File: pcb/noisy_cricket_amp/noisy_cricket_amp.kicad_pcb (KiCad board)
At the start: 2 copper layers, 23 parts, among them J1 AudioJack2, J2 AudioJack2, J3 Jack-DC, Q1 MPF102, SW1 SW_SPST, SW2 SW_SPST, U1 LM386

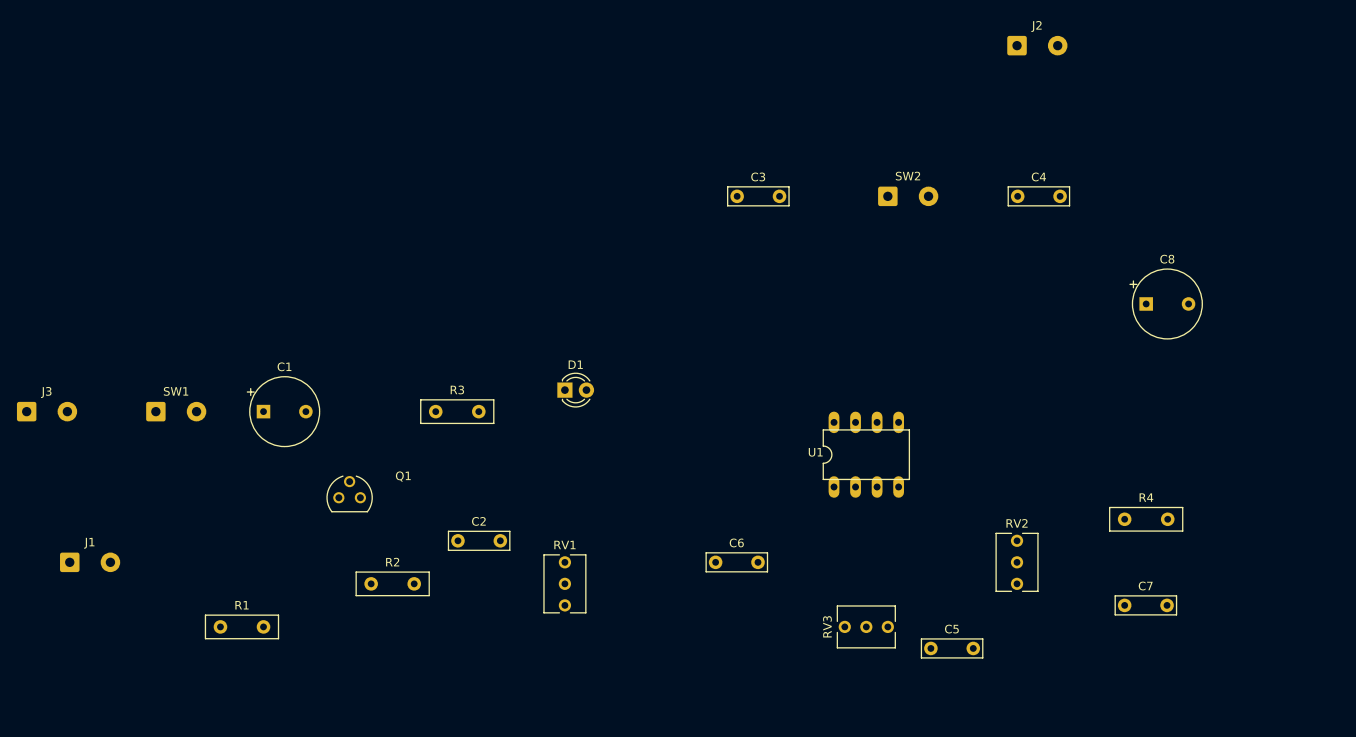
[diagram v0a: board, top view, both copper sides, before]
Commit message: Adding p10 output connector and initial pcb placement
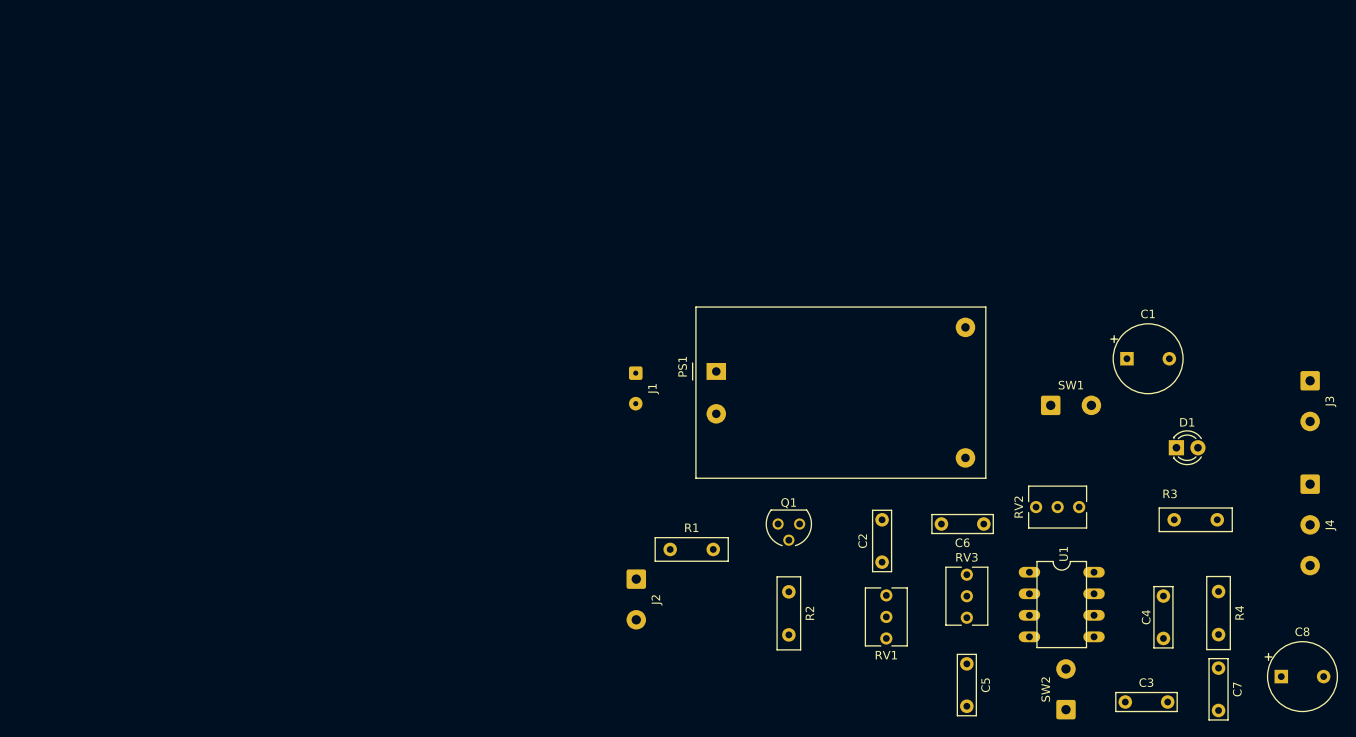
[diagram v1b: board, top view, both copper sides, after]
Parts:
- added J4: AudioJack2_SwitchT, Connector_Wire:SolderWire-0.5sqmm_1x03_P4.8mm_D0.9mm_OD2.3mm, F.Cu at (220.0, 87.3)
- added PS1: HLK-PM12, Converter_ACDC:Converter_ACDC_HiLink_HLK-PMxx, F.Cu at (149.9, 74.0)
- J1: value AudioJack2 -> Conn_01x02_Male; footprint Connector_Wire:SolderWire-0.5sqmm_1x02_P4.8mm_D0.9mm_OD2.3mm -> Connector_Wire:SolderWire-0.1sqmm_1x02_P3.6mm_D0.4mm_OD1mm
- J3: value Jack-DC -> AudioJack2
- moved J3 151.5 mm to (220.0, 75.1), turned to -90 degrees
- moved SW1 105.6 mm to (189.4, 78.0)
- moved C1 102.1 mm to (198.4, 72.5)
- moved R3 88.1 mm to (204.0, 91.5)
- moved J2 77.3 mm to (140.5, 98.5), turned to -90 degrees
- moved C3 75.2 mm to (198.2, 113.0)
- moved D1 72.5 mm to (204.2, 83.0)
- moved J1 70.4 mm to (140.4, 74.2), turned to -90 degrees
- moved SW2 64.1 mm to (191.2, 113.9), turned to 90 degrees
- moved C4 54.9 mm to (202.7, 105.5), turned to 90 degrees
- moved R1 53.8 mm to (144.5, 95.0)
- moved Q1 51.9 mm to (158.5, 92.0), turned to 180 degrees
- moved C2 50.1 mm to (169.5, 96.5), turned to 90 degrees
- moved R2 49.3 mm to (158.5, 100.0), turned to -90 degrees
- moved C8 46.8 mm to (216.6, 110.0)
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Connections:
- J2 pad T: Net-(C8-Pad2) -> Net-(J2-PadT)
- Q1 pad 3: Net-(Q1-Pad3) -> Net-(J2-PadT)
- R1 pad 1: Net-(Q1-Pad3) -> Net-(J2-PadT)
- SW1 pad 1: Net-(J3-Pad1) -> Net-(PS1-Pad4)

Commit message: Routing component trails
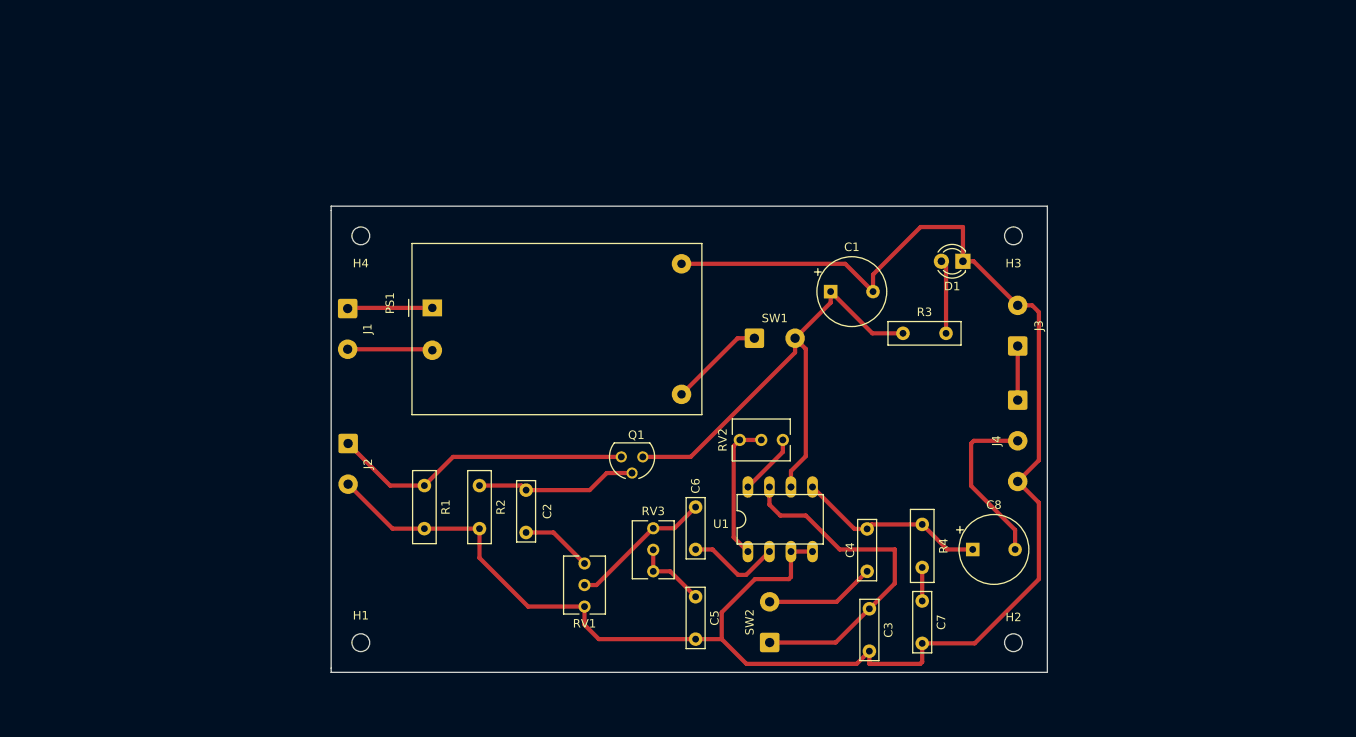
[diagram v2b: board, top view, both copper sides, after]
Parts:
- added H1: MountingHole, MountingHole:MountingHole_2.1mm, F.Cu at (108.0, 106.0)
- added H2: MountingHole, MountingHole:MountingHole_2.1mm, F.Cu at (185.0, 106.0)
- added H3: MountingHole, MountingHole:MountingHole_2.1mm, F.Cu at (185.0, 58.0)
- added H4: MountingHole, MountingHole:MountingHole_2.1mm, F.Cu at (108.0, 58.0)
- J1: footprint Connector_Wire:SolderWire-0.1sqmm_1x02_P3.6mm_D0.4mm_OD1mm -> Connector_Wire:SolderWire-0.5sqmm_1x02_P4.8mm_D0.9mm_OD2.3mm
- moved C2 42.1 mm to (127.5, 93.0)
- moved C8 39.4 mm to (180.2, 95.0)
- moved R3 38.8 mm to (172.0, 69.5)
- moved R2 38.6 mm to (122.0, 87.5)
- moved J2 37.6 mm to (106.5, 82.5)
- moved RV3 37.4 mm to (142.5, 92.5)
- moved J4 35.9 mm to (185.5, 77.4)
- moved C1 35.8 mm to (163.4, 64.6)
- moved RV2 35.8 mm to (152.7, 82.1)
- moved SW1 35.8 mm to (154.4, 70.1)
- moved C4 35.8 mm to (167.7, 97.6)
- moved C7 35.8 mm to (174.2, 101.1)
- moved R4 35.8 mm to (174.2, 92.0)
- moved SW2 35.8 mm to (156.2, 106.0)
- moved RV1 35.8 mm to (134.4, 101.7)
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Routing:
- net GND: track 0.00 -> 207.7 mm
- net Net-(C1-Pad1): track 0.00 -> 61.7 mm
- net Net-(C3-Pad1): track 0.00 -> 42.0 mm
- net Net-(J2-PadT): track 0.00 -> 35.7 mm
- net Net-(C4-Pad2): track 0.00 -> 22.4 mm
- net Net-(C8-Pad2): track 0.00 -> 20.3 mm
- net Net-(C2-Pad2): track 0.00 -> 19.1 mm
- net Net-(C6-Pad2): track 0.00 -> 16.9 mm
- net Net-(RV2-Pad1): track 0.00 -> 16.7 mm
- net Net-(C4-Pad1): track 0.00 -> 13.0 mm
- net Net-(PS1-Pad4): track 0.00 -> 11.3 mm
- net Net-(C6-Pad1): track 0.00 -> 11.1 mm
- net Net-(J1-Pad2): track 0.00 -> 10.0 mm
- net Net-(J1-Pad1): track 0.00 -> 10.0 mm
- net Net-(C5-Pad1): track 0.00 -> 8.78 mm
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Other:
- board outline added: 84.5 x 55 mm

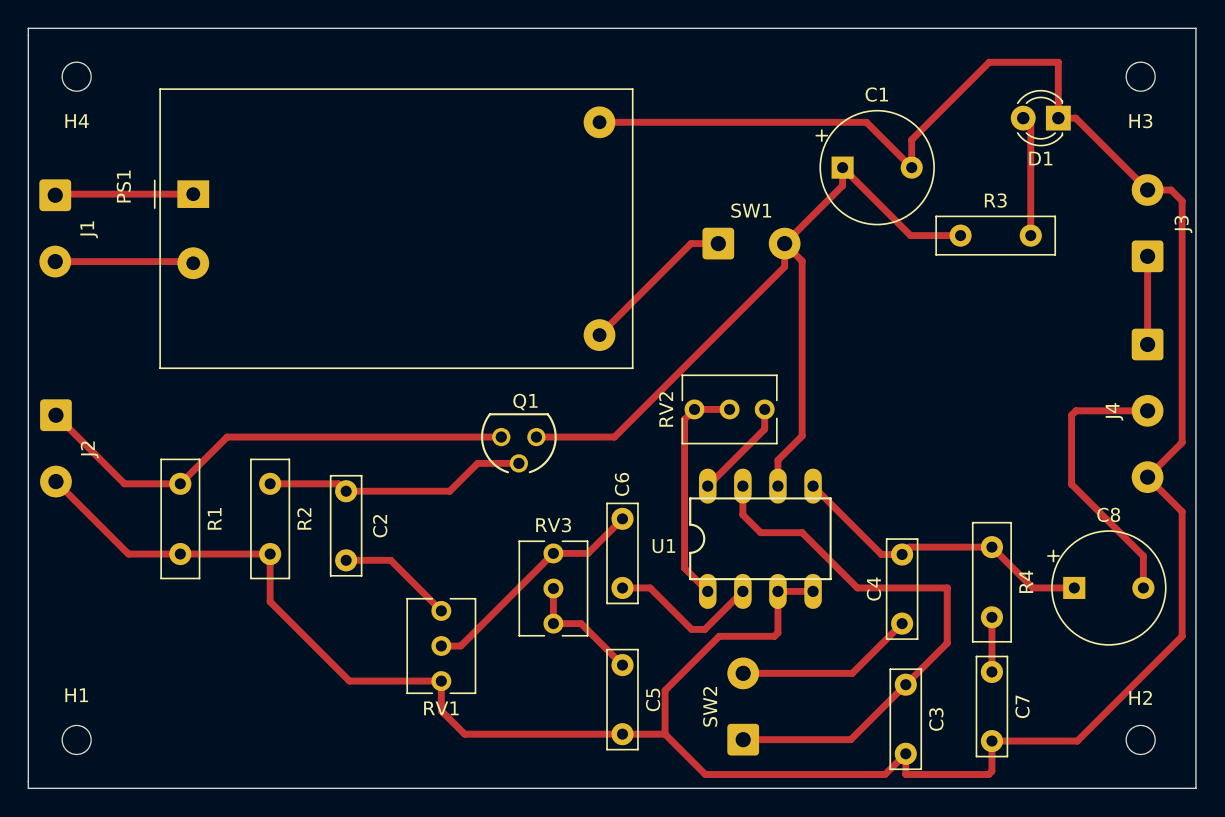
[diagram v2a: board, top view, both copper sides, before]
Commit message: Holes for battery and layout improvements
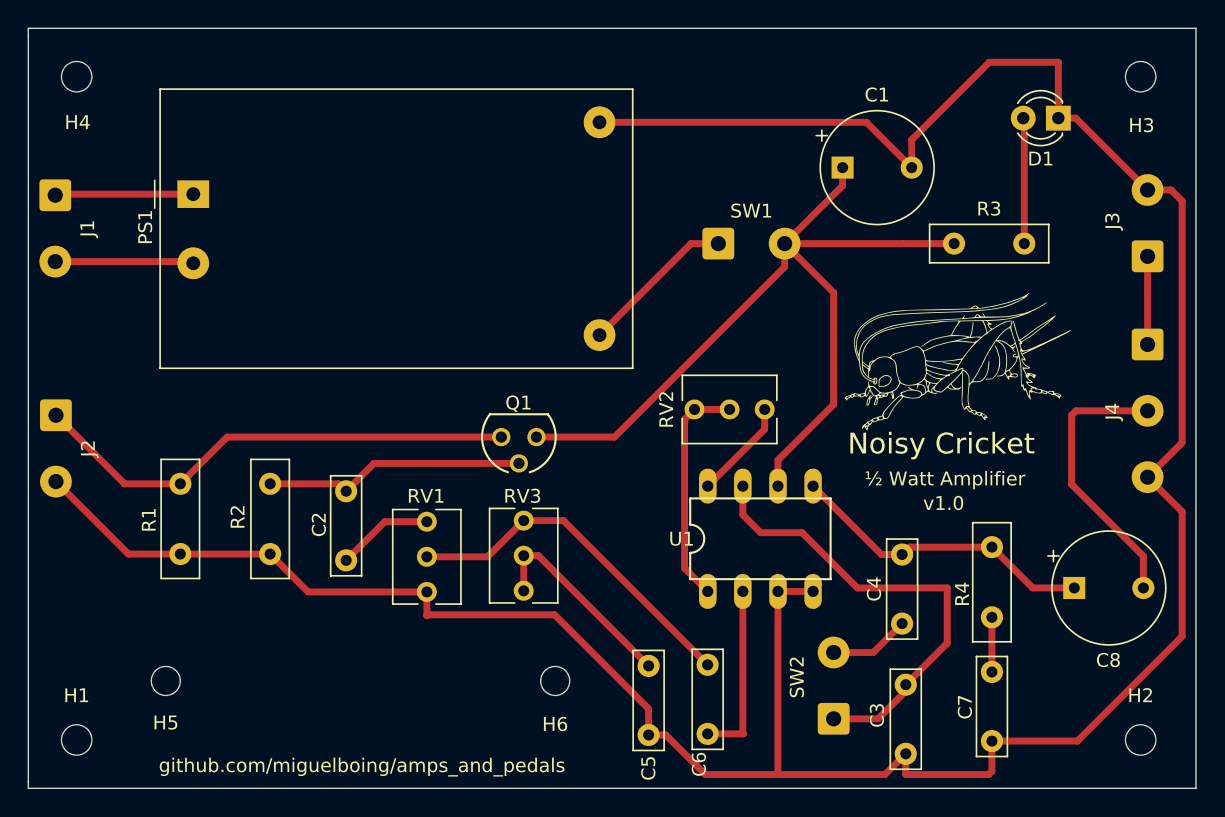
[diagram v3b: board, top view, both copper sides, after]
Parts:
- added G***: LOGO, logo:logo, F.Cu at (171.5, 79.4)
- added H5: MountingHole_Pad, MountingHole:MountingHole_2.1mm, F.Cu at (114.5, 101.7)
- added H6: MountingHole_Pad, MountingHole:MountingHole_2.1mm, F.Cu at (142.6, 101.7)
- H1, H2, H3, H4: footprint MountingHole:MountingHole_2.1mm -> MountingHole:MountingHole_2.2mm_M2
- moved C6 12.2 mm to (153.7, 105.6)
- moved SW2 6.72 mm to (162.8, 104.5)
- moved RV1 6.54 mm to (133.3, 95.3)
- moved RV3 3.20 mm to (140.3, 90.1)
- moved C5 1.89 mm to (149.4, 100.6)
- moved R3 0.75 mm to (171.5, 70.1)
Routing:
- net Net-(C6-Pad2): track 16.9 -> 25.7 mm
- net Net-(C3-Pad1): track 42.0 -> 33.8 mm
- net Net-(C4-Pad1): track 13.0 -> 5.82 mm
- net Net-(C5-Pad1): track 8.78 -> 14.9 mm
- net GND: track 207.7 -> 203.8 mm
- net Net-(C1-Pad1): track 61.7 -> 64.8 mm
- net Net-(C6-Pad1): track 11.1 -> 12.9 mm
- net Net-(C2-Pad1): track 8.41 -> 7.00 mm
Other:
- board text added: "Noisy Cricket"
- board text added: "github.com/miguelboing/amps_and_pedals"
- board text added: "v1.0"
- board text added: "½ Watt Amplifier"
